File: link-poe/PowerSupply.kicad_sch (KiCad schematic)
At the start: 8 parts, among them U501 TPSM33625

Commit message: Update usb + link-poe
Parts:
- C501: footprint Capacitor_SMD:C_1210_3225Metric -> V2_Capacitor_SMD:C_1210; symbol Device:C_Small -> V2_Device:C_1210_10u; Mouser (none) -> 810-CNA6P1X7R1H106K2
- C502: footprint Capacitor_SMD:C_0603_1608Metric -> V2_Capacitor_SMD:C_0603; symbol Device:C_Small -> V2_Device:C_0603_0u1; Mouser (none) -> 810-CGA3E2X7R1H104MA
- C503, C504: footprint Capacitor_SMD:C_1210_3225Metric -> V2_Capacitor_SMD:C_1210; symbol Device:C_Small -> V2_Device:C_1210_22u; Mouser (none) -> 810-CGA6P3X7R1E226M5
- C505: footprint Capacitor_SMD:C_0603_1608Metric -> V2_Capacitor_SMD:C_0603; symbol Device:C_Small -> V2_Device:C_0603_1u; Mouser (none) -> 810-CGA3E2X7R1H104MA
- R501: footprint Resistor_SMD:R_0603_1608Metric -> V2_Resistor_SMD:R_0603; symbol Device:R_Small -> V2_Device:R_0603_40k2; Mouser (none) -> 71-RCS060340K2FKEA
- R502: footprint Resistor_SMD:R_0603_1608Metric -> V2_Resistor_SMD:R_0603; symbol Device:R_Small -> V2_Device:R_0603_10k; Mouser (none) -> 71-CRCW060310K0FKEAC
- U501: Mouser (none) -> 595-TPSM33625RDNR
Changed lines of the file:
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@@
+			)
+		)
+		(property "Mouser" "595-TPSM33625RDNR"
+			(at 148.59 102.87 0)
+			(effects
+				(font
+					(size 1.27 1.27)
+				)
+				(hide yes)
 			)
 		)
@@
 	)
 	(symbol
-		(lib_id "Device:C_Small")
+		(lib_id "V2_Device:C_0603_0u1")
 		(at 109.22 97.79 0)
 		(unit 1)
@@
 			)
 		)
-		(property "Footprint" "Capacitor_SMD:C_0603_1608Metric"
+		(property "Footprint" "V2_Capacitor_SMD:C_0603"
+			(at 109.22 114.808 0)
+			(effects
+				(font
+					(size 1.27 1.27)
+				)
+				(hide yes)
+			)
+		)
+		(property "Datasheet" ""
 			(at 109.22 97.79 0)
 			(effects
@@
 			)
 		)
-		(property "Datasheet" "~"
-			(at 109.22 97.79 0)
-			(effects
-				(font
-					(size 1.27 1.27)
-				)
-				(hide yes)
-			)
-		)
 		(property "Description" "Unpolarized capacitor, small symbol"
-			(at 109.22 97.79 0)
+			(at 109.22 111.252 0)
+			(effects
+				(font
+					(size 1.27 1.27)
+				)
+				(hide yes)
+			)
+		)
+		(property "Mouser" "810-CGA3E2X7R1H104MA"
+			(at 109.22 115.062 0)
 			(effects
 				(font
@@
 	)
 	(symbol
-		(lib_id "Device:C_Small")
+		(lib_id "V2_Device:C_1210_22u")
 		(at 195.58 97.79 0)
 		(unit 1)
@@
 			)
 		)
-		(property "Footprint" "Capacitor_SMD:C_1210_3225Metric"
+		(property "Footprint" "V2_Capacitor_SMD:C_1210"
+			(at 195.58 114.808 0)
+			(effects
+				(font
+					(size 1.27 1.27)
+				)
+				(hide yes)
+			)
+		)
+		(property "Datasheet" ""
 			(at 195.58 97.79 0)
 			(effects
@@
 			)
 		)
-		(property "Datasheet" "~"
-			(at 195.58 97.79 0)
-			(effects
-				(font
-					(size 1.27 1.27)
-				)
-				(hide yes)
-			)
-		)
 		(property "Description" "Unpolarized capacitor, small symbol"
-			(at 195.58 97.79 0)
+			(at 195.58 111.252 0)
+			(effects
+				(font
+					(size 1.27 1.27)
+				)
+				(hide yes)
+			)
+		)
+		(property "Mouser" "810-CGA6P3X7R1E226M5"
+			(at 195.58 114.3 0)
 			(effects
 				(font
@@
 	)
 	(symbol
-		(lib_id "Device:R_Small")
+		(lib_id "V2_Device:R_0603_40k2")
 		(at 172.72 97.79 0)
 		(unit 1)
@@
 			)
 		)
-		(property "Footprint" "Resistor_SMD:R_0603_1608Metric"
+		(property "Footprint" "V2_Resistor_SMD:R_0603"
+			(at 172.72 113.538 0)
+			(effects
+				(font
+					(size 1.27 1.27)
+				)
+				(hide yes)
+			)
+		)
+		(property "Datasheet" ""
 			(at 172.72 97.79 0)
 			(effects
@@
 			)
 		)
-		(property "Datasheet" "~"
-			(at 172.72 97.79 0)
-			(effects
-				(font
-					(size 1.27 1.27)
-				)
-				(hide yes)
-			)
-		)
 		(property "Description" "Resistor, small symbol"
-			(at 172.72 97.79 0)
+			(at 172.72 109.982 0)
+			(effects
+				(font
+					(size 1.27 1.27)
+				)
+				(hide yes)
+			)
+		)
+		(property "Mouser" "71-RCS060340K2FKEA"
+			(at 172.72 113.284 0)
 			(effects
 				(font
@@
 	)
 	(symbol
-		(lib_id "Device:C_Small")
+		(lib_id "V2_Device:C_0603_1u")
 		(at 128.27 107.95 0)
 		(unit 1)
@@
 			)
 		)
-		(property "Footprint" "Capacitor_SMD:C_0603_1608Metric"
+		(property "Footprint" "V2_Capacitor_SMD:C_0603"
+			(at 128.27 124.968 0)
+			(effects
+				(font
+					(size 1.27 1.27)
+				)
+				(hide yes)
+			)
+		)
+		(property "Datasheet" ""
 			(at 128.27 107.95 0)
 			(effects
@@
 			)
 		)
-		(property "Datasheet" "~"
-			(at 128.27 107.95 0)
-			(effects
-				(font
-					(size 1.27 1.27)
-				)
-				(hide yes)
-			)
-		)
 		(property "Description" "Unpolarized capacitor, small symbol"
-			(at 128.27 107.95 0)
+			(at 128.27 121.412 0)
+			(effects
+				(font
+					(size 1.27 1.27)
+				)
+				(hide yes)
+			)
+		)
+		(property "Mouser" "810-CGA3E2X7R1H104MA"
+			(at 128.27 125.222 0)
 			(effects
 				(font
@@
 	)
 	(symbol
-		(lib_id "Device:C_Small")
+		(lib_id "V2_Device:C_1210_22u")
 		(at 185.42 97.79 0)
 		(unit 1)
@@
 			)
 		)
-		(property "Footprint" "Capacitor_SMD:C_1210_3225Metric"
+		(property "Footprint" "V2_Capacitor_SMD:C_1210"
+			(at 185.42 114.808 0)
+			(effects
+				(font
+					(size 1.27 1.27)
+				)
+				(hide yes)
+			)
+		)
+		(property "Datasheet" ""
 			(at 185.42 97.79 0)
 			(effects
@@
 			)
 		)
-		(property "Datasheet" "~"
-			(at 185.42 97.79 0)
-			(effects
-				(font
-					(size 1.27 1.27)
-				)
-				(hide yes)
-			)
-		)
 		(property "Description" "Unpolarized capacitor, small symbol"
-			(at 185.42 97.79 0)
+			(at 185.42 111.252 0)
+			(effects
+				(font
+					(size 1.27 1.27)
+				)
+				(hide yes)
+			)
+		)
+		(property "Mouser" "810-CGA6P3X7R1E226M5"
+			(at 185.42 114.3 0)
 			(effects
 				(font
@@
 	)
 	(symbol
-		(lib_id "Device:R_Small")
+		(lib_id "V2_Device:R_0603_10k")
 		(at 172.72 102.87 0)
 		(unit 1)
@@
 			)
 		)
-		(property "Footprint" "Resistor_SMD:R_0603_1608Metric"
+		(property "Footprint" "V2_Resistor_SMD:R_0603"
+			(at 172.72 118.618 0)
+			(effects
+				(font
+					(size 1.27 1.27)
+				)
+				(hide yes)
+			)
+		)
+		(property "Datasheet" ""
 			(at 172.72 102.87 0)
 			(effects
@@
 			)
 		)
-		(property "Datasheet" "~"
-			(at 172.72 102.87 0)
-			(effects
-				(font
-					(size 1.27 1.27)
-				)
-				(hide yes)
-			)
-		)
 		(property "Description" "Resistor, small symbol"
-			(at 172.72 102.87 0)
+			(at 172.72 115.062 0)
+			(effects
+				(font
+					(size 1.27 1.27)
+				)
+				(hide yes)
+			)
+		)
+		(property "Mouser" "71-CRCW060310K0FKEAC"
+			(at 172.72 119.126 0)
 			(effects
 				(font
@@
 	)
 	(symbol
-		(lib_id "Device:C_Small")
+		(lib_id "V2_Device:C_1210_10u")
 		(at 97.79 97.79 0)
 		(unit 1)
@@
 			)
 		)
-		(property "Footprint" "Capacitor_SMD:C_1210_3225Metric"
+		(property "Footprint" "V2_Capacitor_SMD:C_1210"
+			(at 97.79 114.808 0)
+			(effects
+				(font
+					(size 1.27 1.27)
+				)
+				(hide yes)
+			)
+		)
+		(property "Datasheet" ""
 			(at 97.79 97.79 0)
 			(effects
@@
 			)
 		)
-		(property "Datasheet" "~"
-			(at 97.79 97.79 0)
-			(effects
-				(font
-					(size 1.27 1.27)
-				)
-				(hide yes)
-			)
-		)
 		(property "Description" "Unpolarized capacitor, small symbol"
-			(at 97.79 97.79 0)
-			(effects
-				(font
+			(at 97.79 111.252 0)
+			(effects
+				(font
+					(size 1.27 1.27)
+				)
+				(hide yes)
+			)
+		)
+		(property "Mouser" "810-CNA6P1X7R1H106K2"
+			(at 97.79 114.3 0)
+			(effects
+				(font

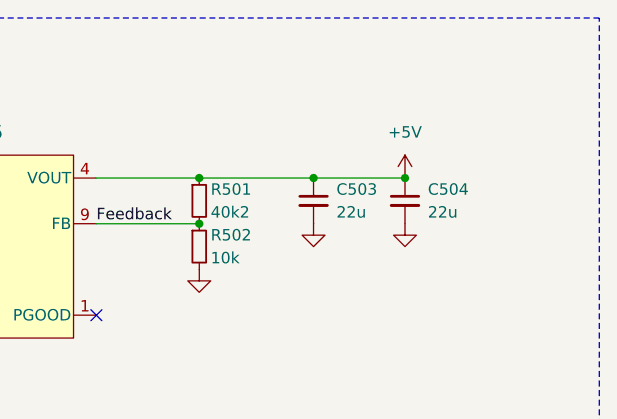
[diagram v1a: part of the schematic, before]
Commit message: Update power symbols
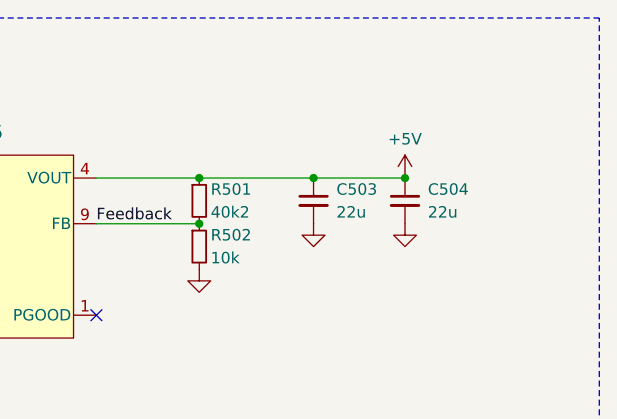
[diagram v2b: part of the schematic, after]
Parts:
- C501: Rating (none) -> 50V
- C503, C504: Rating (none) -> 25V
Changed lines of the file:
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@@
+			)
+		)
+		(property "Rating" "25V"
+			(at 195.58 117.094 0)
+			(effects
+				(font
+					(size 1.27 1.27)
+				)
+				(hide yes)
 			)
 		)
@@
 	)
 	(symbol
-		(lib_id "power:GND")
+		(lib_id "V2_power:GND")
 		(at 185.42 100.33 0)
 		(unit 1)
@@
 		)
 		(property "Value" "GND"
-			(at 185.42 105.41 0)
+			(at 185.42 104.394 0)
 			(effects
 				(font
@@
 		)
 		(property "Description" "Power symbol creates a global label with name \"GND\" , ground"
-			(at 185.42 100.33 0)
+			(at 185.166 110.744 0)
 			(effects
 				(font
@@
 	)
 	(symbol
-		(lib_id "power:GND")
+		(lib_id "V2_power:GND")
 		(at 195.58 100.33 0)
 		(unit 1)
@@
 		)
 		(property "Value" "GND"
-			(at 195.58 105.41 0)
+			(at 195.58 104.394 0)
 			(effects
 				(font
@@
 		)
 		(property "Description" "Power symbol creates a global label with name \"GND\" , ground"
-			(at 195.58 100.33 0)
+			(at 195.326 110.744 0)
 			(effects
 				(font
@@
 	)
 	(symbol
-		(lib_id "power:+5V")
+		(lib_id "V2_power:+5V")
 		(at 195.58 95.25 0)
 		(unit 1)
@@
 		)
 		(property "Value" "+5V"
-			(at 195.58 90.17 0)
+			(at 195.58 90.932 0)
 			(effects
 				(font
@@
 		)
 		(property "Description" "Power symbol creates a global label with name \"+5V\""
-			(at 195.58 95.25 0)
+			(at 195.58 109.728 0)
 			(effects
 				(font
@@
 	)
 	(symbol
-		(lib_id "power:GND")
+		(lib_id "V2_power:GND")
 		(at 97.79 100.33 0)
 		(unit 1)
@@
 		)
 		(property "Value" "GND"
-			(at 97.79 104.775 0)
+			(at 97.79 104.394 0)
 			(effects
 				(font
@@
 		)
 		(property "Description" "Power symbol creates a global label with name \"GND\" , ground"
-			(at 97.79 100.33 0)
+			(at 97.536 110.744 0)
 			(effects
 				(font
@@
 	)
 	(symbol
-		(lib_id "power:GND")
+		(lib_id "V2_power:GND")
 		(at 172.72 105.41 0)
 		(unit 1)
@@
 		)
 		(property "Value" "GND"
-			(at 172.72 110.49 0)
+			(at 172.72 109.474 0)
 			(effects
 				(font
@@
 		)
 		(property "Description" "Power symbol creates a global label with name \"GND\" , ground"
-			(at 172.72 105.41 0)
+			(at 172.466 115.824 0)
 			(effects
 				(font
@@
 	)
 	(symbol
-		(lib_id "power:GND")
+		(lib_id "V2_power:GND")
 		(at 109.22 100.33 0)
 		(unit 1)
@@
 		)
 		(property "Value" "GND"
-			(at 109.22 105.41 0)
+			(at 109.22 104.394 0)
 			(effects
 				(font
@@
 		)
 		(property "Description" "Power symbol creates a global label with name \"GND\" , ground"
-			(at 109.22 100.33 0)
+			(at 108.966 110.744 0)
 			(effects
 				(font
@@
 			)
 		)
+		(property "Rating" "25V"
+			(at 189.738 101.6 0)
+			(effects
+				(font
+					(size 1.27 1.27)
+				)
+				(hide yes)
+			)
+		)
 		(pin "1"
 		)
@@
 	)
 	(symbol
-		(lib_id "power:GND")
+		(lib_id "V2_power:GND")
 		(at 128.27 110.49 0)
 		(unit 1)
@@
 		)
 		(property "Value" "GND"
-			(at 128.27 115.57 90)
+			(at 128.27 114.554 0)
 			(effects
 				(font
@@
 		)
 		(property "Description" "Power symbol creates a global label with name \"GND\" , ground"
-			(at 128.27 110.49 0)
+			(at 128.016 120.904 0)
 			(effects
 				(font
@@
 	)
 	(symbol
-		(lib_id "power:GND")
+		(lib_id "V2_power:GND")
 		(at 148.59 115.57 0)
 		(unit 1)
@@
 		)
 		(property "Value" "GND"
-			(at 148.59 120.65 0)
+			(at 148.59 119.634 0)
 			(effects
 				(font
@@
 		)
 		(property "Description" "Power symbol creates a global label with name \"GND\" , ground"
-			(at 148.59 115.57 0)
+			(at 148.336 125.984 0)
 			(effects
 				(font
@@
 			(effects
 				(font
+					(size 1.27 1.27)
+				)
+				(hide yes)
+			)
+		)
+		(property "Rating" "50V"
+			(at 102.108 102.108 0)
+			(effects
+				(font

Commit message: Update parts
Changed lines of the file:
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@@
 	(wire
 		(pts
-			(xy 80.01 95.25) (xy 97.79 95.25)
+			(xy 82.55 95.25) (xy 97.79 95.25)
 		)
 		(stroke
@@
 	(polyline
 		(pts
-			(xy 78.74 77.47) (xy 78.74 133.35)
+			(xy 82.55 77.47) (xy 82.55 133.35)
 		)
 		(stroke
@@
 	(polyline
 		(pts
-			(xy 78.74 133.35) (xy 217.17 133.35)
+			(xy 82.55 133.35) (xy 217.17 133.35)
 		)
 		(stroke
@@
 	(polyline
 		(pts
-			(xy 217.17 77.47) (xy 78.74 77.47)
+			(xy 217.17 77.47) (xy 82.55 77.47)
 		)
 		(stroke
@@
 	(hierarchical_label "Input"
 		(shape input)
-		(at 80.01 95.25 180)
+		(at 82.55 95.25 180)
 		(effects
 			(font
@@
 		)
 		(property "Value" "+5V"
-			(at 195.58 90.932 0)
-			(effects
-				(font
+			(at 195.58 90.678 0)
+			(effects
+				(font

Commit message: Refresh
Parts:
- C501: Manufacturer (none) -> TDK; Product (none) -> CNA6P1X7R1H106K250AE; Rating 50V -> (none); Voltage (none) -> 50V
- C502: Manufacturer (none) -> TDK; Product (none) -> CGA3E2X7R1H104M080AA
- C503, C504: Manufacturer (none) -> TDK; Product (none) -> CGA6P3X7R1E226M250AE; Rating 25V -> (none); Voltage (none) -> 25V
- C505: Manufacturer (none) -> YAGEO; Mouser 810-CGA3E2X7R1H104MA -> 603-CC603KRX7R9BB105; Product (none) -> CC0603KRX7R9BB105
- R501: Manufacturer (none) -> Vishay; Product (none) -> RCS060340K2FKEA; Rating (none) -> 500mW
- R502: Manufacturer (none) -> Vishay; Product (none) -> CRCW060310K0FKEAC; Rating (none) -> 100mW
- U501: Manufacturer (none) -> Texas Instruments; Product (none) -> TPSM33625RDNR
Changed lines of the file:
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@@
+			)
+		)
+		(property "Manufacturer" "Texas Instruments"
+			(at 148.59 146.05 0)
+			(effects
+				(font
+					(size 1.27 1.27)
+				)
+				(hide yes)
+			)
+		)
+		(property "Product" "TPSM33625RDNR"
+			(at 148.59 148.59 0)
+			(effects
+				(font
+					(size 1.27 1.27)
+				)
+				(hide yes)
 			)
 		)
@@
 			)
 		)
+		(property "Manufacturer" "TDK"
+			(at 109.22 113.03 0)
+			(effects
+				(font
+					(size 1.27 1.27)
+				)
+				(hide yes)
+			)
+		)
+		(property "Product" "CGA3E2X7R1H104M080AA"
+			(at 109.22 115.57 0)
+			(effects
+				(font
+					(size 1.27 1.27)
+				)
+				(hide yes)
+			)
+		)
 		(pin "1"
 		)
@@
 			)
 		)
-		(property "Rating" "25V"
-			(at 195.58 117.094 0)
+		(property "Voltage" "25V"
+			(at 195.58 118.11 0)
+			(effects
+				(font
+					(size 1.27 1.27)
+				)
+				(hide yes)
+			)
+		)
+		(property "Product" "CGA6P3X7R1E226M250AE"
+			(at 195.58 115.57 0)
+			(effects
+				(font
+					(size 1.27 1.27)
+				)
+				(hide yes)
+			)
+		)
+		(property "Manufacturer" "TDK"
+			(at 195.58 113.03 0)
 			(effects
 				(font
@@
 			)
 		)
+		(property "Rating" "500mW"
+			(at 172.72 118.11 0)
+			(effects
+				(font
+					(size 1.27 1.27)
+				)
+				(hide yes)
+			)
+		)
+		(property "Manufacturer" "Vishay"
+			(at 172.72 113.03 0)
+			(effects
+				(font
+					(size 1.27 1.27)
+				)
+				(hide yes)
+			)
+		)
+		(property "Product" "RCS060340K2FKEA"
+			(at 172.72 115.57 0)
+			(effects
+				(font
+					(size 1.27 1.27)
+				)
+				(hide yes)
+			)
+		)
 		(pin "1"
 		)
@@
 			)
 		)
-		(property "Mouser" "810-CGA3E2X7R1H104MA"
+		(property "Mouser" "603-CC603KRX7R9BB105"
 			(at 128.27 125.222 0)
+			(effects
+				(font
+					(size 1.27 1.27)
+				)
+				(hide yes)
+			)
+		)
+		(property "Product" "CC0603KRX7R9BB105"
+			(at 128.27 125.73 0)
+			(effects
+				(font
+					(size 1.27 1.27)
+				)
+				(hide yes)
+			)
+		)
+		(property "Manufacturer" "YAGEO"
+			(at 128.27 123.19 0)
 			(effects
 				(font
@@
 			)
 		)
-		(property "Rating" "25V"
-			(at 189.738 101.6 0)
+		(property "Voltage" "25V"
+			(at 185.42 118.11 0)
+			(effects
+				(font
+					(size 1.27 1.27)
+				)
+				(hide yes)
+			)
+		)
+		(property "Product" "CGA6P3X7R1E226M250AE"
+			(at 185.42 115.57 0)
+			(effects
+				(font
+					(size 1.27 1.27)
+				)
+				(hide yes)
+			)
+		)
+		(property "Manufacturer" "TDK"
+			(at 185.42 113.03 0)
 			(effects
 				(font
@@
 			)
 		)
+		(property "Product" "CRCW060310K0FKEAC"
+			(at 172.72 120.65 0)
+			(effects
+				(font
+					(size 1.27 1.27)
+				)
+				(hide yes)
+			)
+		)
+		(property "Manufacturer" "Vishay"
+			(at 172.72 118.11 0)
+			(effects
+				(font
+					(size 1.27 1.27)
+				)
+				(hide yes)
+			)
+		)
+		(property "Rating" "100mW"
+			(at 172.72 123.19 0)
+			(effects
+				(font
+					(size 1.27 1.27)
+				)
+				(hide yes)
+			)
+		)
 		(pin "1"
 		)
@@
 			)
 		)
-		(property "Rating" "50V"
-			(at 102.108 102.108 0)
-			(effects
-				(font
+		(property "Voltage" "50V"
+			(at 97.79 118.11 0)
+			(effects
+				(font
+					(size 1.27 1.27)
+				)
+				(hide yes)
+			)
+		)
+		(property "Product" "CNA6P1X7R1H106K250AE"
+			(at 97.79 115.57 0)
+			(effects
+				(font
+					(size 1.27 1.27)
+				)
+				(hide yes)
+			)
+		)
+		(property "Manufacturer" "TDK"
+			(at 97.79 113.03 0)
+			(effects
+				(font

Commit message: Fix WAGOs
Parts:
- C505: Rating (none) -> 50V
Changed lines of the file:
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@@
+			)
+		)
+		(property "Rating" "50V"
+			(at 128.27 130.81 0)
+			(effects
+				(font
+					(size 1.27 1.27)
+				)
+				(hide yes)
 			)
 		)

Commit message: Refresh
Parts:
- C501: Rating (none) -> 50V; Voltage 50V -> (none)
- C502: Rating (none) -> 50V
- C503, C504: Rating (none) -> 25V; Voltage 25V -> (none)
- C505: Manufacturer YAGEO -> TDK; Mouser 603-CC603KRX7R9BB105 -> 810-CGA3E3X7R1H105K0; Product CC0603KRX7R9BB105 -> CGA3E3X7R1H105K080AB
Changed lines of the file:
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@@
+			)
+		)
+		(property "Rating" "50V"
+			(at 109.22 120.65 0)
+			(effects
+				(font
+					(size 1.27 1.27)
+				)
+				(hide yes)
 			)
 		)
@@
 			)
 		)
-		(property "Voltage" "25V"
-			(at 195.58 118.11 0)
-			(effects
-				(font
-					(size 1.27 1.27)
-				)
-				(hide yes)
-			)
-		)
 		(property "Product" "CGA6P3X7R1E226M250AE"
 			(at 195.58 115.57 0)
@@
 			)
 		)
+		(property "Rating" "25V"
+			(at 195.58 118.11 0)
+			(effects
+				(font
+					(size 1.27 1.27)
+				)
+				(hide yes)
+			)
+		)
 		(pin "1"
 		)
@@
 			)
 		)
-		(property "Mouser" "603-CC603KRX7R9BB105"
+		(property "Mouser" "810-CGA3E3X7R1H105K0"
 			(at 128.27 125.222 0)
 			(effects
@@
 			)
 		)
-		(property "Product" "CC0603KRX7R9BB105"
+		(property "Product" "CGA3E3X7R1H105K080AB"
 			(at 128.27 125.73 0)
 			(effects
@@
 			)
 		)
-		(property "Manufacturer" "YAGEO"
+		(property "Manufacturer" "TDK"
 			(at 128.27 123.19 0)
 			(effects
@@
 			)
 		)
-		(property "Voltage" "25V"
-			(at 185.42 118.11 0)
-			(effects
-				(font
-					(size 1.27 1.27)
-				)
-				(hide yes)
-			)
-		)
 		(property "Product" "CGA6P3X7R1E226M250AE"
 			(at 185.42 115.57 0)
@@
 			)
 		)
+		(property "Rating" "25V"
+			(at 185.42 118.11 0)
+			(effects
+				(font
+					(size 1.27 1.27)
+				)
+				(hide yes)
+			)
+		)
 		(pin "1"
 		)
@@
 			)
 		)
-		(property "Voltage" "50V"
-			(at 97.79 118.11 0)
-			(effects
-				(font
-					(size 1.27 1.27)
-				)
-				(hide yes)
-			)
-		)
 		(property "Product" "CNA6P1X7R1H106K250AE"
 			(at 97.79 115.57 0)
@@
 			(effects
 				(font
+					(size 1.27 1.27)
+				)
+				(hide yes)
+			)
+		)
+		(property "Rating" "50V"
+			(at 97.79 118.11 0)
+			(effects
+				(font

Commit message: Use date as revision
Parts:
- U501: value TPSM33625 -> TPSM33625RDNR; footprint V2_Converter_DCDC:TPSM33625 -> V2_Converter_DCDC:QFN-11; symbol V2_Converter_DCDC:TPSM33625 -> V2_Converter_DCDC:TPSM33625RDNR; Rating (none) -> 2.5A
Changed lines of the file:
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@@
 	)
 	(symbol
-		(lib_id "V2_Converter_DCDC:TPSM33625")
+		(lib_id "V2_Converter_DCDC:TPSM33625RDNR")
 		(at 148.59 102.87 0)
 		(unit 1)
@@
 			)
 		)
-		(property "Value" "TPSM33625"
+		(property "Value" "TPSM33625RDNR"
 			(at 144.78 90.17 0)
 			(effects
@@
 			)
 		)
-		(property "Footprint" "V2_Converter_DCDC:TPSM33625"
+		(property "Footprint" "V2_Converter_DCDC:QFN-11"
 			(at 148.59 118.11 0)
 			(effects
@@
 			)
 		)
-		(property "Datasheet" "https://www.ti.com/lit/ds/symlink/tpsm33625.pdf"
+		(property "Datasheet" ""
 			(at 153.67 118.11 0)
 			(effects
@@
 			)
 		)
+		(property "Rating" "2.5A"
+			(at 148.59 153.67 0)
+			(effects
+				(font
+					(size 1.27 1.27)
+				)
+				(hide yes)
+			)
+		)
 		(pin "1"
 		)
@@
 			)
 		)
-		(property "Description" "Power symbol creates a global label with name \"GND\" , ground"
+		(property "Description" ""
 			(at 185.166 110.744 0)
 			(effects
@@
 			)
 		)
-		(property "Description" "Power symbol creates a global label with name \"GND\" , ground"
+		(property "Description" ""
 			(at 195.326 110.744 0)
 			(effects
@@
 			)
 		)
-		(property "Description" "Power symbol creates a global label with name \"+5V\""
+		(property "Description" ""
 			(at 195.58 109.728 0)
 			(effects
@@
 			)
 		)
-		(property "Description" "Power symbol creates a global label with name \"GND\" , ground"
+		(property "Description" ""
 			(at 97.536 110.744 0)
 			(effects
@@
 			)
 		)
-		(property "Description" "Power symbol creates a global label with name \"GND\" , ground"
+		(property "Description" ""
 			(at 172.466 115.824 0)
 			(effects
@@
 			)
 		)
-		(property "Description" "Power symbol creates a global label with name \"GND\" , ground"
+		(property "Description" ""
 			(at 108.966 110.744 0)
 			(effects
@@
 			)
 		)
-		(property "Description" "Power symbol creates a global label with name \"GND\" , ground"
+		(property "Description" ""
 			(at 128.016 120.904 0)
 			(effects
@@
 			)
 		)
-		(property "Description" "Power symbol creates a global label with name \"GND\" , ground"
+		(property "Description" ""
 			(at 148.336 125.984 0)
 			(effects
